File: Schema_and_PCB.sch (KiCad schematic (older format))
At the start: 0 parts

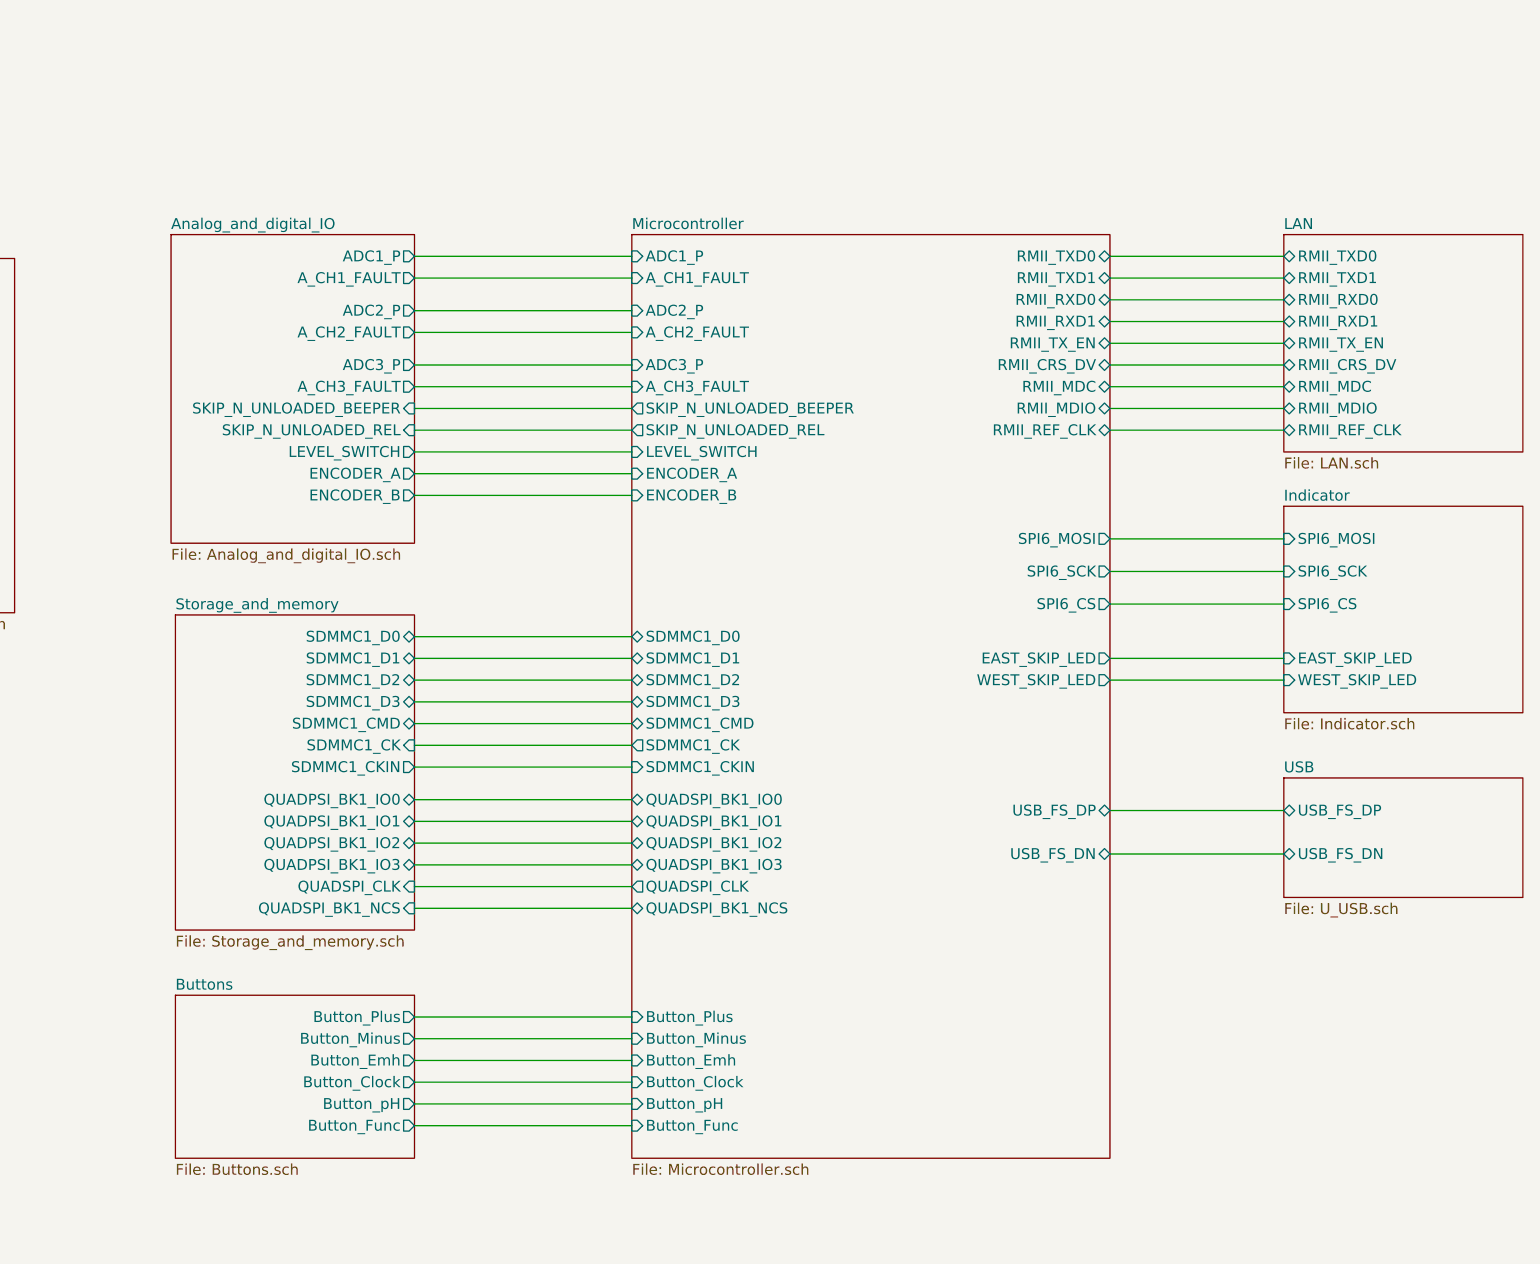
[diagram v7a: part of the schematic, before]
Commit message: deleted TXS0206 added SN74AVCA406DGGR and corrected schema for it
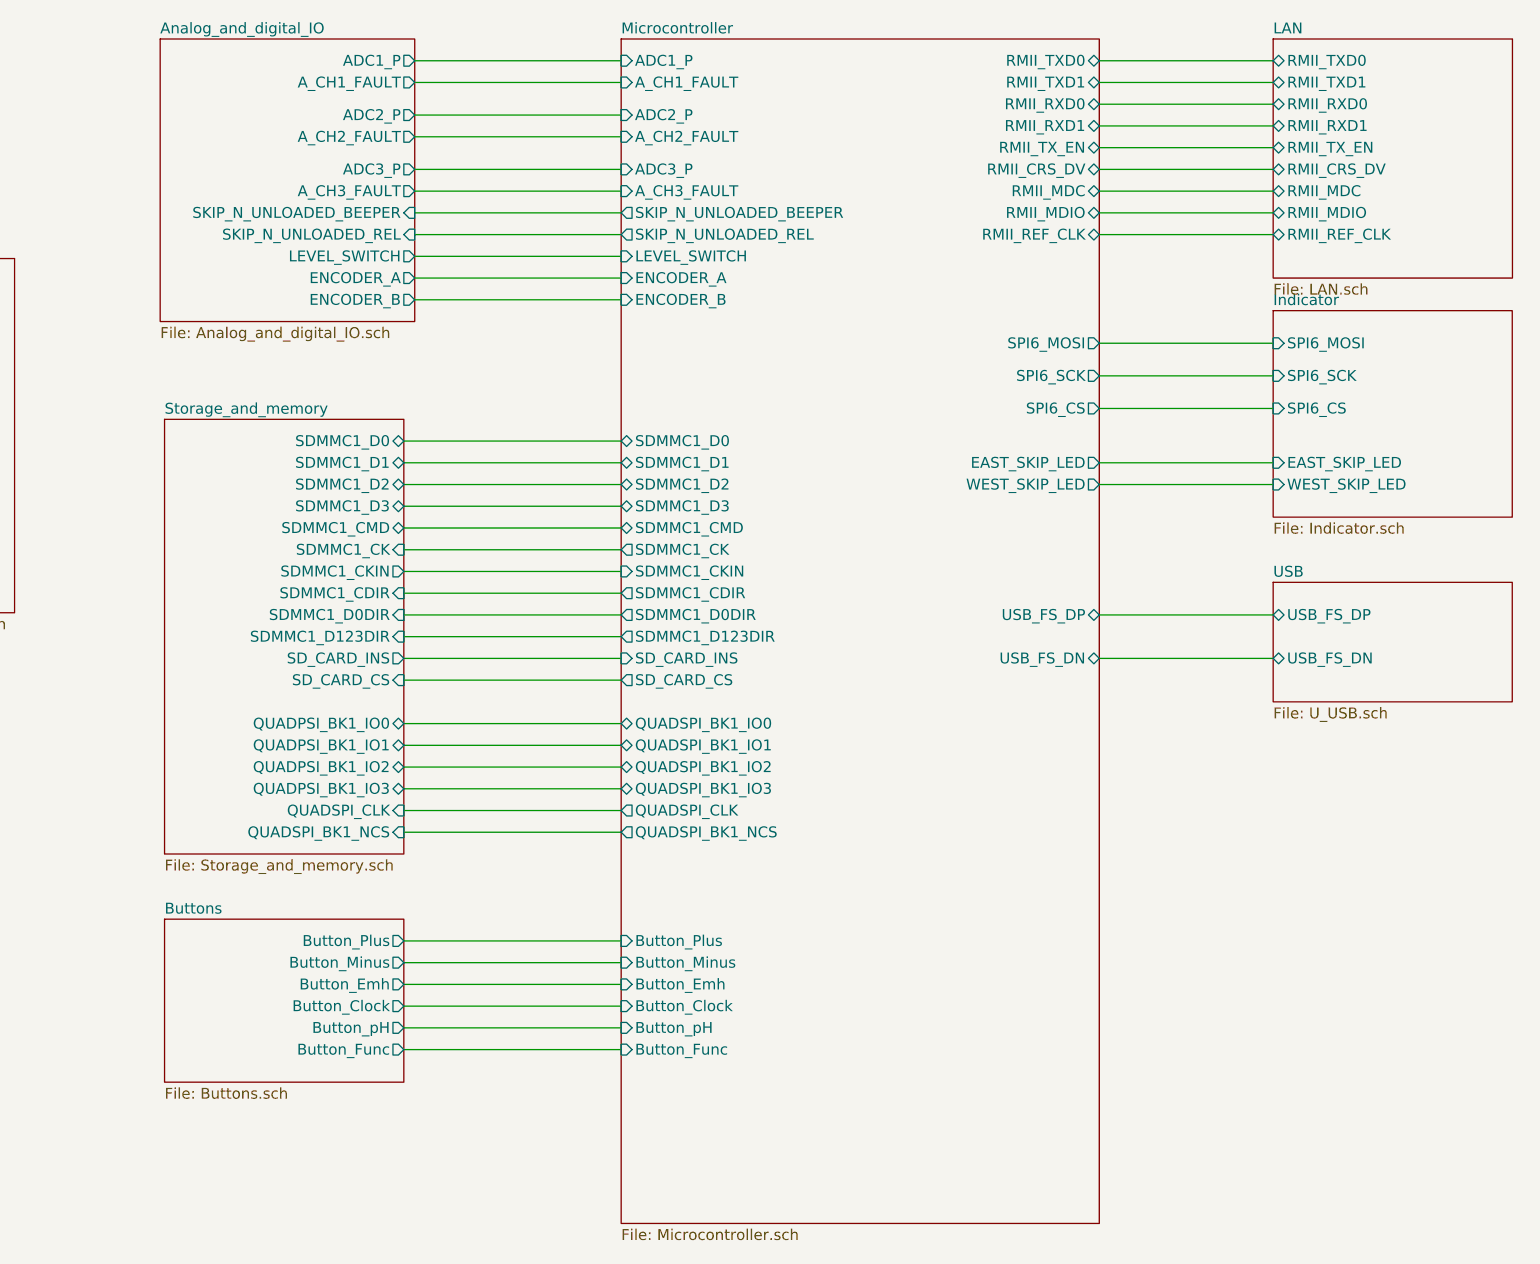
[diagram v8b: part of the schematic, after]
